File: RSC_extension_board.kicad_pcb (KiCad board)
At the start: 2 copper layers, 34 parts, among them J1 Conn_01x03, J10 Conn_01x02, J2 Conn_01x03, J3 Raspberry_Pi_4, J4 Conn_01x04, J5 Conn_01x03, J6 Conn_01x02, J7 Conn_01x03, J8 PRT-14417, J9 USB_C_Receptacle_PowerOnly_6P, Q1 BSS138, Q2 2N7002-7-F, SW1 SW_Wuerth_450301014042, U1 USBLC6-2SC6

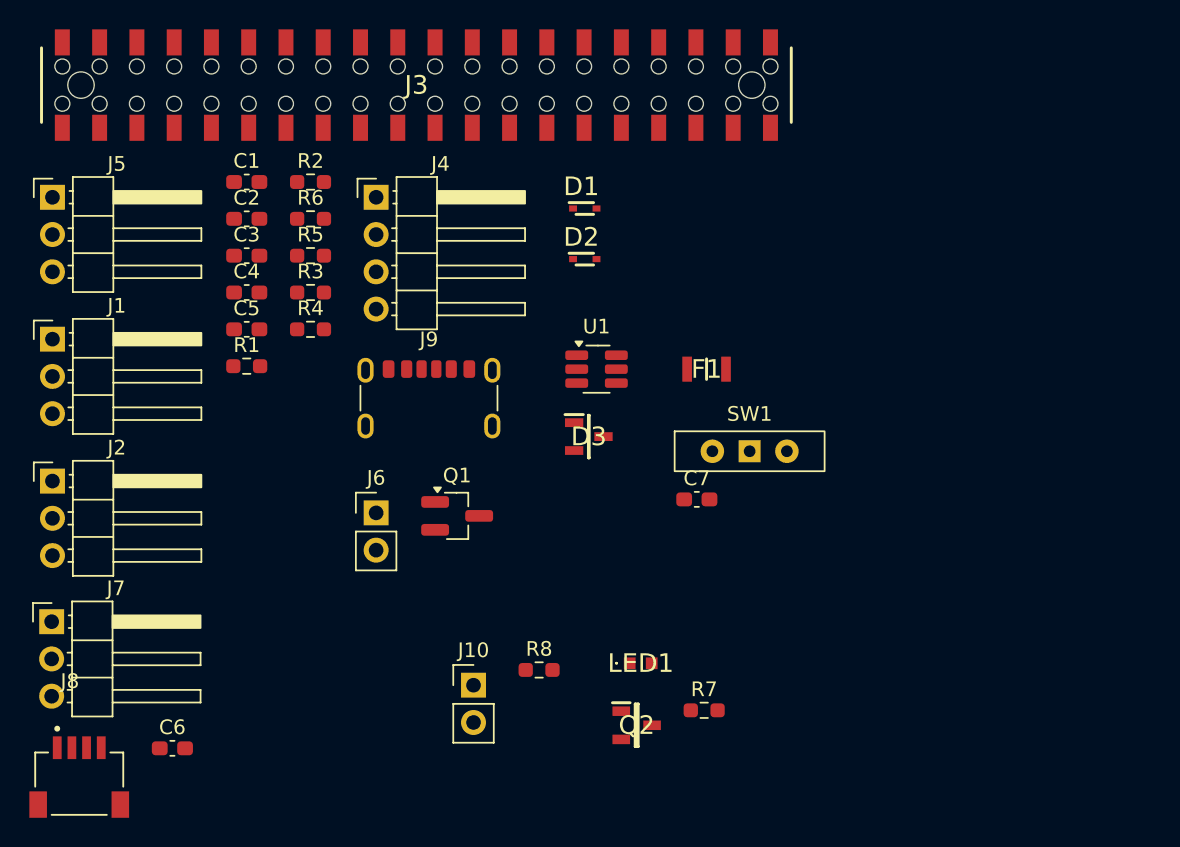
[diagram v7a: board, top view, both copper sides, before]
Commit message: spi display pinout change. button connector simplified.
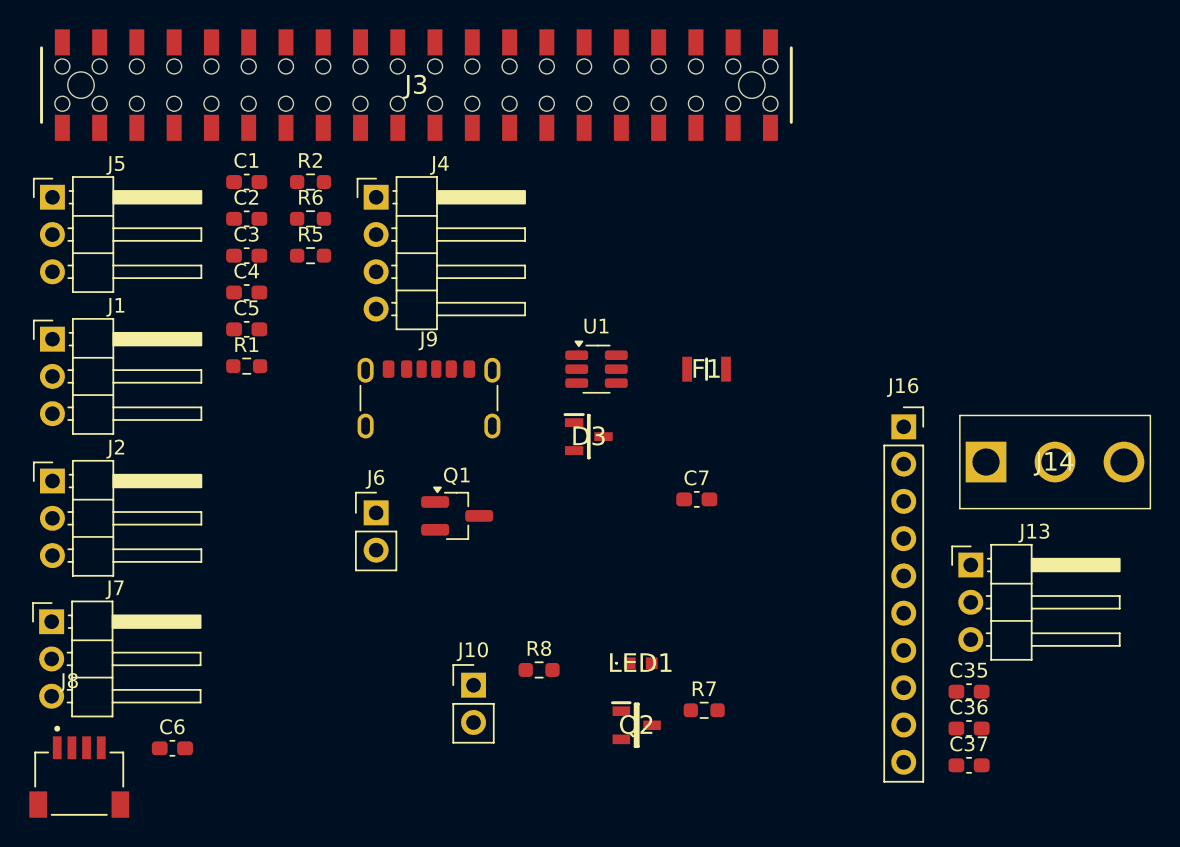
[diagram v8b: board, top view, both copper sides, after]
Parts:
- removed D1, D2: PJSD03TS-AU_R1_000A1, PJSD03TS-AU_R1_000A1:SODFL1608X65N
- removed R3, R4: 10k, Resistor_SMD:R_0603_1608Metric_Pad0.98x0.95mm_HandSolder
- removed SW1: SW_Wuerth_450301014042, Button_Switch_THT:SW_Slide-03_Wuerth-WS-SLTV_10x2.5x6.4_P2.54mm
- added C35: 100nF, Capacitor_SMD:C_0603_1608Metric_Pad1.08x0.95mm_HandSolder, F.Cu at (161.9, 91.0)
- added C36: 100nF, Capacitor_SMD:C_0603_1608Metric_Pad1.08x0.95mm_HandSolder, F.Cu at (161.9, 93.5)
- added C37: 100nF, Capacitor_SMD:C_0603_1608Metric_Pad1.08x0.95mm_HandSolder, F.Cu at (161.9, 96.0)
- added J13: Conn_01x03, Connector_PinHeader_2.54mm:PinHeader_1x03_P2.54mm_Horizontal, F.Cu at (162.0, 82.3)
- added J14: 500SSP1S2M2QEA, 500SSP1S2M2QEA:500SSP1S2M2QEA, F.Cu at (163.0, 75.3)
- added J16: Conn_01x10, Connector_PinSocket_2.54mm:PinSocket_1x10_P2.54mm_Vertical, F.Cu at (157.4, 72.9)
- J9: footprint Connector_USB:USB_C_Receptacle_GCT_USB4125-xx-x_6P_TopMnt_Horizontal -> Connector_USB:USB_C_Receptacle_GCT_USB4125-xx-x-0190_6P_TopMnt_Horizontal
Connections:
- D3 pad 3: Net-(U1-VBUS) -> Net-(D3-Pad3)
- F1 pad 1: Net-(U1-VBUS) -> Net-(D3-Pad3)
- J10 pad 1: Net-(J10-Pin_1) -> +5V
- J10 pad 2: +5V -> Net-(J10-Pin_2)
- J3 pad 13: unconnected-(J3-GPIO27/SDIO_DAT3-Pad13) -> /SPI_DC
- J3 pad 15: unconnected-(J3-GPIO22/SDIO_CLK-Pad15) -> /LCD_BL
- J3 pad 16: unconnected-(J3-GPIO23/SDIO_CMD-Pad16) -> /BUTTON
- J3 pad 18: unconnected-(J3-GPIO24/SDIO_DAT0-Pad18) -> /LED_PWM
- J3 pad 19: unconnected-(J3-MOSI_SPI0/GPIO10-Pad19) -> /SPI_MOSI
- J3 pad 21: /LED_3.3V -> /SPI_MISO
- J3 pad 23: unconnected-(J3-SCLK_SPI0/GPIO11-Pad23) -> /SPI_CLK
- J3 pad 24: unconnected-(J3-~{CE0}_SPI0/GPIO08-Pad24) -> /SPI_CS
- J3 pad 29: /M1_PWM -> unconnected-(J3-GPCLK1/GPIO05-Pad29)
- J3 pad 31: /M2_PWM -> /LED_3.3V
- J3 pad 32: unconnected-(J3-GPIO12/PWM0-Pad32) -> /M1_PWM
- J3 pad 33: unconnected-(J3-GPIO13/PWM1-Pad33) -> /M2_PWM
- J3 pad 37: /BUTTON -> /M3_PWM
- J3 pad 7: unconnected-(J3-GPCLK0/GPIO04-Pad7) -> /SPI_RST
- J6 pad 1: Net-(D2-K) -> /BUTTON
- J8 pad S1: (no net) -> Earth
- J8 pad S2: (no net) -> Earth
- J9 pad A9: Net-(U1-VBUS) -> Net-(D3-Pad3)
- J9 pad B9: Net-(U1-VBUS) -> Net-(D3-Pad3)
- Q2 pad 3: Net-(J10-Pin_1) -> Net-(J10-Pin_2)
- R8 pad 2: /SOME_GPIO_with_pwm -> /LED_PWM
- U1 pad 5: Net-(U1-VBUS) -> unconnected-(U1-VBUS-Pad5)
